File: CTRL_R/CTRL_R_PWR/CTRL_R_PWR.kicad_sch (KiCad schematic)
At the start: 24 parts, among them J1 BM14B-NSHSS-TBT_LF__SN_, J2 BM04B-NSHSS-TBT_LF__SN_, J3 5051100592, U2 74LVC1G08

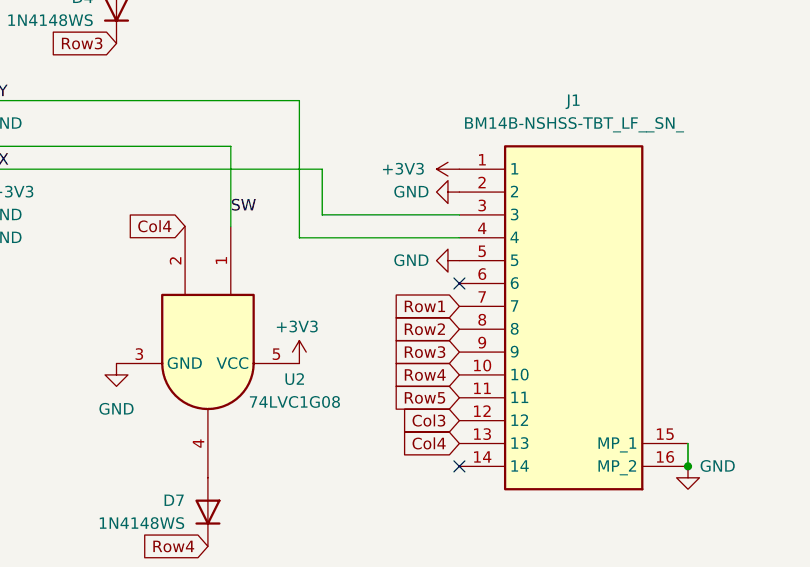
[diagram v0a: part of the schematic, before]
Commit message: Created CTRL_R_PWR Placeholder files
Also removed unnecessary "PWR_Button" Global Label in CTRL_R
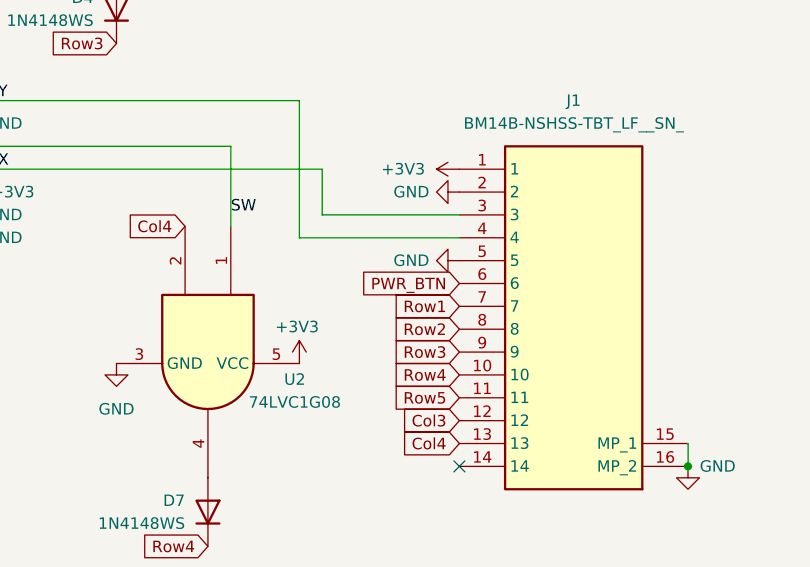
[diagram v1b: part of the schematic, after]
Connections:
- net PWR_BTN: now reaches J1.6
- no-connect marks 2 -> 1
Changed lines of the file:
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@@
 		(at 158.75 128.27)
 	)
-	(no_connect
-		(at 158.75 107.95)
-	)
 	(wire
 		(pts
@@
 		)
 	)
+	(global_label "PWR_BTN"
+		(shape input)
+		(at 158.75 107.95 180)
+		(fields_autoplaced yes)
+		(effects
+			(font
+				(size 1.27 1.27)
+			)
+			(justify right)
+		)
+		(property "Intersheetrefs" "${INTERSHEET_REFS}"
+			(at 147.2377 107.95 0)
+			(hide yes)
+			(show_name no)
+			(do_not_autoplace no)
+			(effects
+				(font
+					(size 1.27 1.27)
+				)
+				(justify right)
+			)
+		)
+	)
 	(global_label "Col3"
 		(shape input)
@@
 		)
 		(instances
-			(project "CTRL_R"
+			(project "CTRL_R_PWR"
 				(path "/8eeed083-de7a-4dfe-ba6c-9e042c3ef75c"
 					(reference "D7")
@@
 		)
 		(instances
-			(project "CTRL_R"
+			(project "CTRL_R_PWR"
 				(path "/8eeed083-de7a-4dfe-ba6c-9e042c3ef75c"
 					(reference "#PWR015")
@@
 		)
 		(instances
-			(project "CTRL_R"
+			(project "CTRL_R_PWR"
 				(path "/8eeed083-de7a-4dfe-ba6c-9e042c3ef75c"
 					(reference "J3")
@@
 		)
 		(instances
-			(project "CTRL_R"
+			(project "CTRL_R_PWR"
 				(path "/8eeed083-de7a-4dfe-ba6c-9e042c3ef75c"
 					(reference "D9")
@@
 		)
 		(instances
-			(project "CTRL_R"
+			(project "CTRL_R_PWR"
 				(path "/8eeed083-de7a-4dfe-ba6c-9e042c3ef75c"
 					(reference "#PWR013")
@@
 		)
 		(instances
-			(project "CTRL_R"
+			(project "CTRL_R_PWR"
 				(path "/8eeed083-de7a-4dfe-ba6c-9e042c3ef75c"
 					(reference "#PWR02")
@@
 		)
 		(instances
-			(project "CTRL_R"
+			(project "CTRL_R_PWR"
 				(path "/8eeed083-de7a-4dfe-ba6c-9e042c3ef75c"
 					(reference "H1")
@@
 		)
 		(instances
-			(project "CTRL_R"
+			(project "CTRL_R_PWR"
 				(path "/8eeed083-de7a-4dfe-ba6c-9e042c3ef75c"
 					(reference "D3")
@@
 		)
 		(instances
-			(project "CTRL_R"
+			(project "CTRL_R_PWR"
 				(path "/8eeed083-de7a-4dfe-ba6c-9e042c3ef75c"
 					(reference "#PWR06")
@@
 		)
 		(instances
-			(project "CTRL_R"
+			(project "CTRL_R_PWR"
 				(path "/8eeed083-de7a-4dfe-ba6c-9e042c3ef75c"
 					(reference "#PWR03")
@@
 		)
 		(instances
-			(project "CTRL_R"
+			(project "CTRL_R_PWR"
 				(path "/8eeed083-de7a-4dfe-ba6c-9e042c3ef75c"
 					(reference "J1")
@@
 		)
 		(instances
-			(project "CTRL_R"
+			(project "CTRL_R_PWR"
 				(path "/8eeed083-de7a-4dfe-ba6c-9e042c3ef75c"
 					(reference "S6")
@@
 		)
 		(instances
-			(project "CTRL_R"
+			(project "CTRL_R_PWR"
 				(path "/8eeed083-de7a-4dfe-ba6c-9e042c3ef75c"
 					(reference "H2")
@@
 		)
 		(instances
-			(project "CTRL_R"
+			(project "CTRL_R_PWR"
 				(path "/8eeed083-de7a-4dfe-ba6c-9e042c3ef75c"
 					(reference "D2")
@@
 		)
 		(instances
-			(project "CTRL_R"
+			(project "CTRL_R_PWR"
 				(path "/8eeed083-de7a-4dfe-ba6c-9e042c3ef75c"
 					(reference "H4")
@@
 		)
 		(instances
-			(project "CTRL_R"
+			(project "CTRL_R_PWR"
 				(path "/8eeed083-de7a-4dfe-ba6c-9e042c3ef75c"
 					(reference "D4")
@@
 		)
 		(instances
-			(project "CTRL_R"
+			(project "CTRL_R_PWR"
 				(path "/8eeed083-de7a-4dfe-ba6c-9e042c3ef75c"
 					(reference "#PWR01")
@@
 		)
 		(instances
-			(project "CTRL_R"
+			(project "CTRL_R_PWR"
 				(path "/8eeed083-de7a-4dfe-ba6c-9e042c3ef75c"
 					(reference "D1")
@@
 		)
 		(instances
-			(project "CTRL_R"
+			(project "CTRL_R_PWR"
 				(path "/8eeed083-de7a-4dfe-ba6c-9e042c3ef75c"
 					(reference "#PWR014")
@@
 		)
 		(instances
-			(project "CTRL_R"
+			(project "CTRL_R_PWR"
 				(path "/8eeed083-de7a-4dfe-ba6c-9e042c3ef75c"
 					(reference "S3")
@@
 		)
 		(instances
-			(project "CTRL_R"
+			(project "CTRL_R_PWR"
 				(path "/8eeed083-de7a-4dfe-ba6c-9e042c3ef75c"
 					(reference "S5")
@@
 		)
 		(instances
-			(project "CTRL_R"
+			(project "CTRL_R_PWR"
 				(path "/8eeed083-de7a-4dfe-ba6c-9e042c3ef75c"
 					(reference "H5")
@@
 		)
 		(instances
-			(project "CTRL_R"
+			(project "CTRL_R_PWR"
 				(path "/8eeed083-de7a-4dfe-ba6c-9e042c3ef75c"
 					(reference "S4")
@@
 		)
 		(instances
-			(project "CTRL_R"
+			(project "CTRL_R_PWR"
 				(path "/8eeed083-de7a-4dfe-ba6c-9e042c3ef75c"
 					(reference "S1")
@@
 		)
 		(instances
-			(project "CTRL_R"
+			(project "CTRL_R_PWR"
 				(path "/8eeed083-de7a-4dfe-ba6c-9e042c3ef75c"
 					(reference "D8")
@@
 		)
 		(instances
-			(project "CTRL_R"
+			(project "CTRL_R_PWR"
 				(path "/8eeed083-de7a-4dfe-ba6c-9e042c3ef75c"
 					(reference "H3")
@@
 		)
 		(instances
-			(project "CTRL_R"
+			(project "CTRL_R_PWR"
 				(path "/8eeed083-de7a-4dfe-ba6c-9e042c3ef75c"
 					(reference "#PWR09")
@@
 		)
 		(instances
-			(project "CTRL_R"
+			(project "CTRL_R_PWR"
 				(path "/8eeed083-de7a-4dfe-ba6c-9e042c3ef75c"
 					(reference "#PWR05")
@@
 		)
 		(instances
-			(project "CTRL_R"
+			(project "CTRL_R_PWR"
 				(path "/8eeed083-de7a-4dfe-ba6c-9e042c3ef75c"
 					(reference "#PWR011")
@@
 		)
 		(instances
-			(project "CTRL_R"
+			(project "CTRL_R_PWR"
 				(path "/8eeed083-de7a-4dfe-ba6c-9e042c3ef75c"
 					(reference "D5")
@@
 		)
 		(instances
-			(project "CTRL_R"
+			(project "CTRL_R_PWR"
 				(path "/8eeed083-de7a-4dfe-ba6c-9e042c3ef75c"
 					(reference "D6")
@@
 		)
 		(instances
-			(project "CTRL_R"
+			(project "CTRL_R_PWR"
 				(path "/8eeed083-de7a-4dfe-ba6c-9e042c3ef75c"
 					(reference "#PWR012")
@@
 		)
 		(instances
-			(project "CTRL_R"
+			(project "CTRL_R_PWR"
 				(path "/8eeed083-de7a-4dfe-ba6c-9e042c3ef75c"
 					(reference "S2")
@@
 		)
 		(instances
-			(project "CTRL_R"
+			(project "CTRL_R_PWR"
 				(path "/8eeed083-de7a-4dfe-ba6c-9e042c3ef75c"
 					(reference "U2")
@@
 		)
 		(instances
-			(project "CTRL_R"
+			(project "CTRL_R_PWR"
 				(path "/8eeed083-de7a-4dfe-ba6c-9e042c3ef75c"
 					(reference "J2")

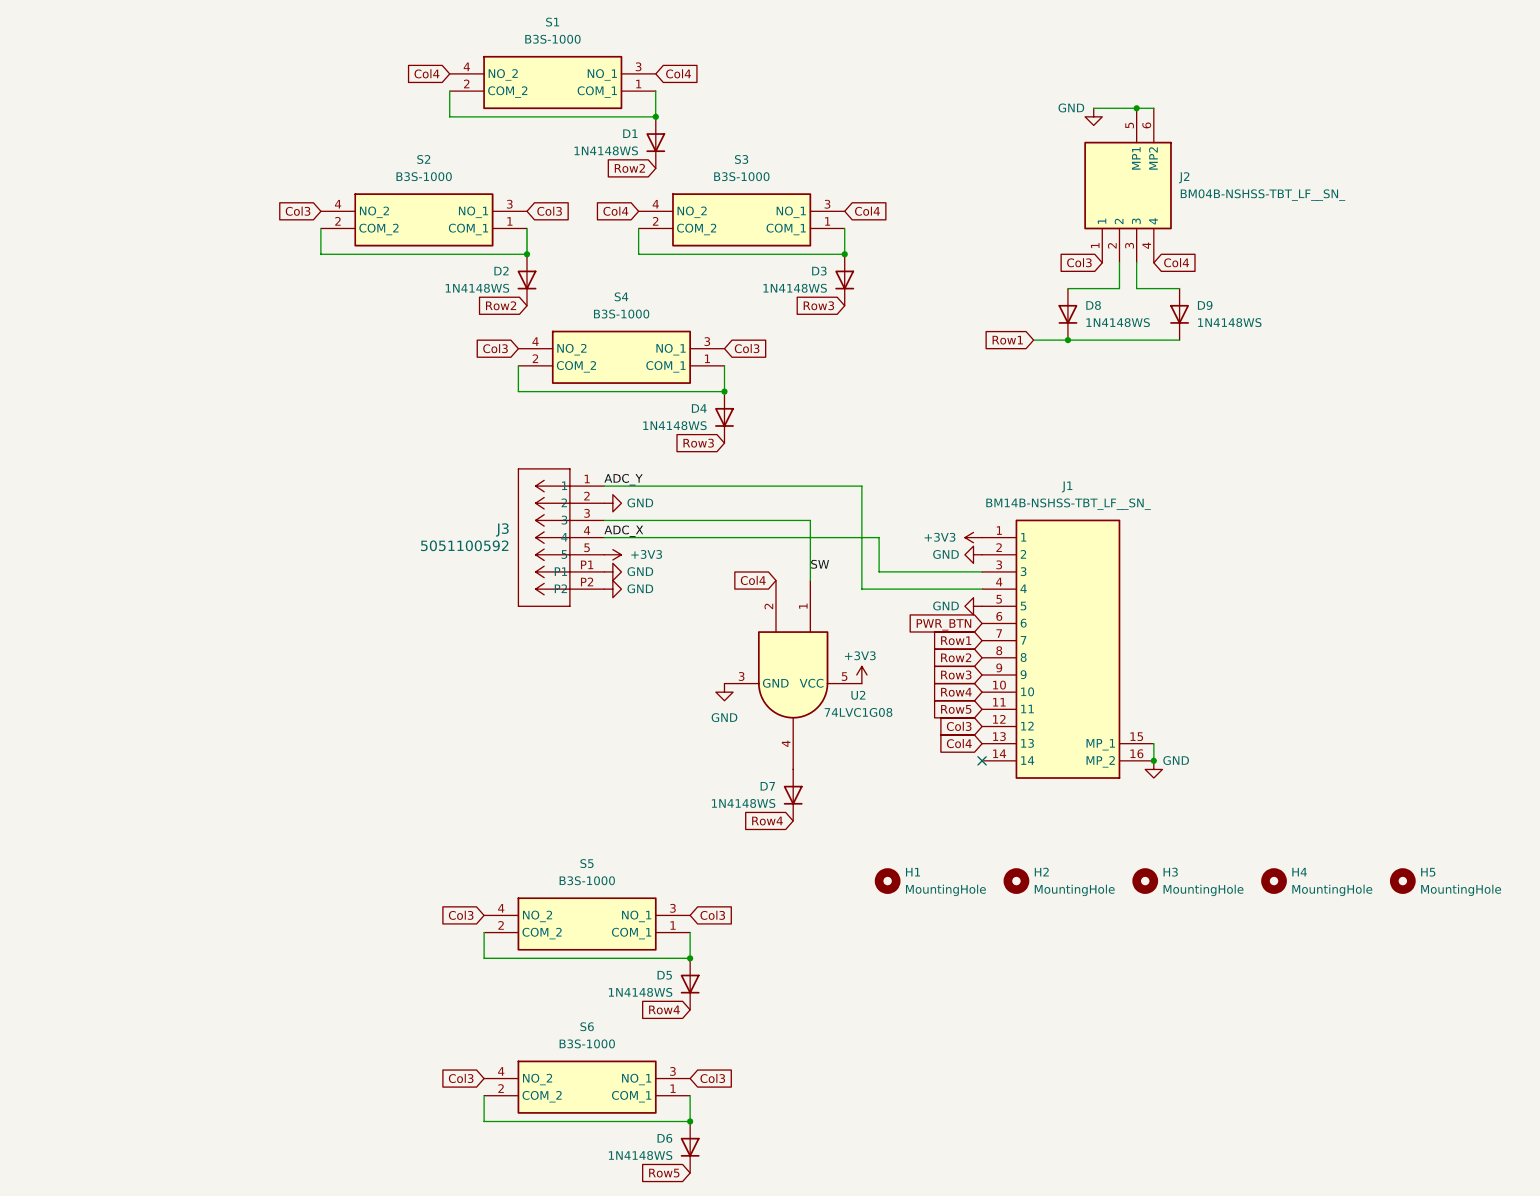
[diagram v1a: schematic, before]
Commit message: CTRL_R_PWR Complete!
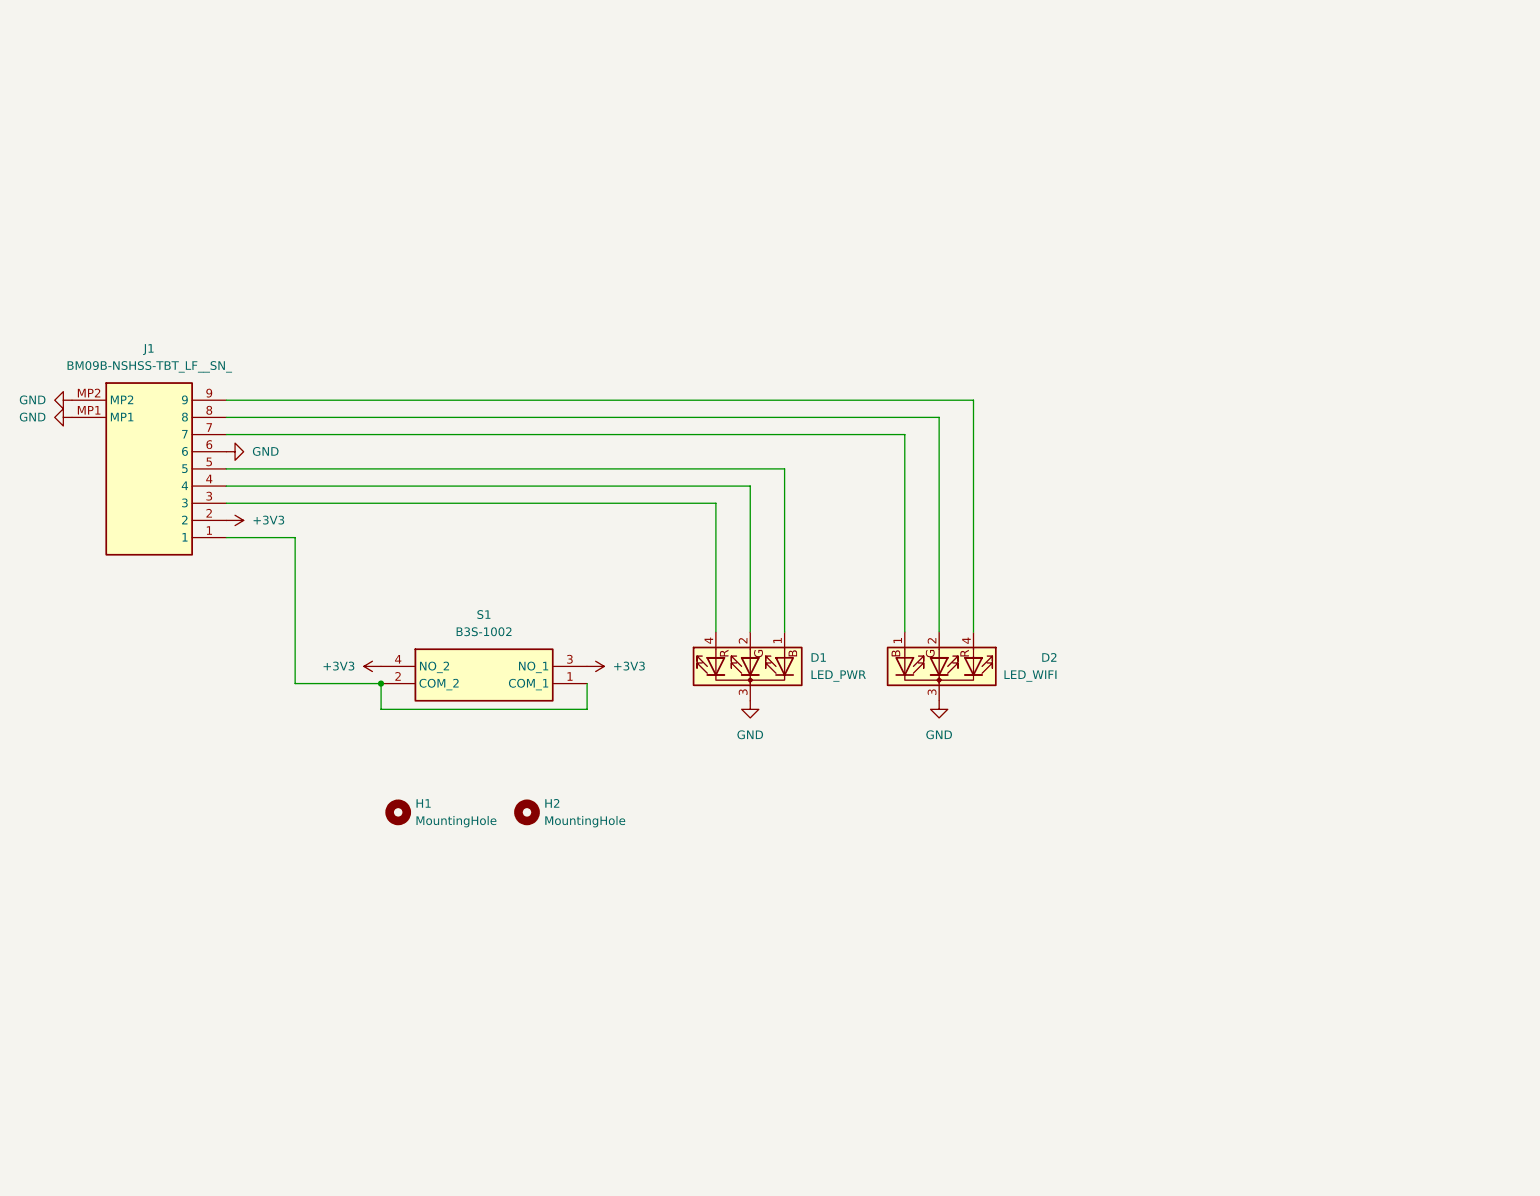
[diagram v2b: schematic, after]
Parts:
- removed D1, D2, D3, D4, D5, D6, D7, D8, D9: 1N4148WS, Diode_SMD:D_SOD-323, symbol Diode:1N4148WS
- removed H3, H4, H5: MountingHole, MountingHole:MountingHole_2.7mm_M2.5, symbol Mechanical:MountingHole
- removed J1: BM14B-NSHSS-TBT_LF__SN_, BM14BNSHSSTBTLFSN, symbol BM14B-NSHSS-TBT_LF__SN_:BM14B-NSHSS-TBT_LF__SN_
- removed J2: BM04B-NSHSS-TBT_LF__SN_, BM04B-NSHSS-TBT:BM04BNSHSSTBTLFSN, symbol BM04B-NSHSS-TBT_LF__SN_:BM04B-NSHSS-TBT_LF__SN_
- removed J3: 5051100592, 5051100592:CON_5051100592_MOL, symbol 5051100592:5051100592
- removed S1, S2, S3, S4, S5, S6: B3S-1000, B3S-1000:B3S1000, symbol B3S-1000:B3S-1000
- removed U2: 74LVC1G08, Package_TO_SOT_SMD:SOT-23-5, symbol 74xGxx:74LVC1G08
- added D1: LED_PWR, LED_THT:LED_D5.0mm-4_RGB, symbol Device:LED_BGKR
- added D2: LED_WIFI, LED_THT:LED_D5.0mm-4_RGB, symbol Device:LED_BGKR
- added J1: BM09B-NSHSS-TBT_LF__SN_, BM09B-NSHSS-TBT_LF__SN_:BM09BNSHSSTBTLFSN, symbol BM09B-NSHSS-TBT_LF__SN_:BM09B-NSHSS-TBT_LF__SN_
- added S1: B3S-1002, B3S-1002:B3S1002, symbol B3S-1002:B3S-1002
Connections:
- net +3V3: now also J1.2, S1.3 (NO_1), S1.4 (NO_2)
- net GND: now also D1.3 (K), D2.3 (K), J1.6, J1.MP1, J1.MP2
- new net: D2.1 (BA), J1.7
- new net: D2.2 (GA), J1.8
- new net: D2.4 (RA), J1.9
- new net: J1.1, S1.1 (COM_1), S1.2 (COM_2)
- new net: D1.1 (BA), J1.5
- new net: D1.2 (GA), J1.4
- new net: D1.4 (RA), J1.3
- no-connect marks 1 -> 0
